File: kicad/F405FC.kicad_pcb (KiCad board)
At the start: 4 copper layers, 36 x 36 mm, 161 parts, among them J1 USB4105-GF-A, J2 ESC, J3 HD VTX, J4 GPS, J5 ELRS, P1 VBAT, P10 LED_DIN, P11 5V, P12 GND, P13 5V, P14 BUZ_N, P15 UART5_TX, P16 UART5_RX, P17 UART6_TX, P18 UART6_RX, P19 MOTOR5, P2 GND, P20 MOTOR6, P21 MOTOR7, P22 MOTOR8, P23 RSSI_IN, P24 GND, P25 5V, P3 10V, P4 GND, P5 CAM1_VID, P6 CAM2_VID, P7 VTX_VID, P8 5V, P9 GND, Q1 PMV40UN2, Q2 NX7002AK, SW1 BOOT, U1 LMR38020FSDDAR, U10 W25N01GV, U11 TS5A3159A, U12 SN74LV1T125, U13 USBLC6-2SC6, U2 LMR38020FSDDAR, U3 STM32F405RGT6, U4 LP38692MP-3.3, U5 LP5907MFX-3.3, U6 ICM-42688-P, U7 BMI270, U8 BMP390, U9 IIS2MDC, Y1 8MHz

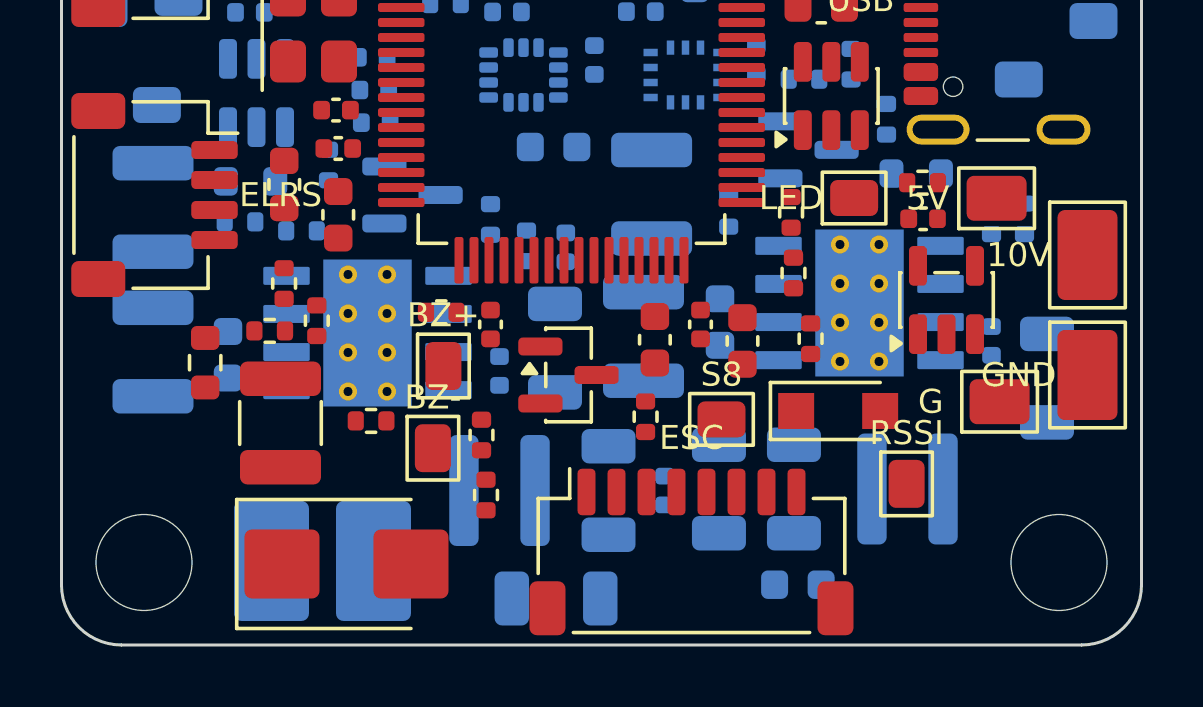
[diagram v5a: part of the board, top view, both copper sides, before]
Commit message: Routing prep: scripted critical buck/VBAT routes (gen/critical.py), BST caps rotated, DRC position helper
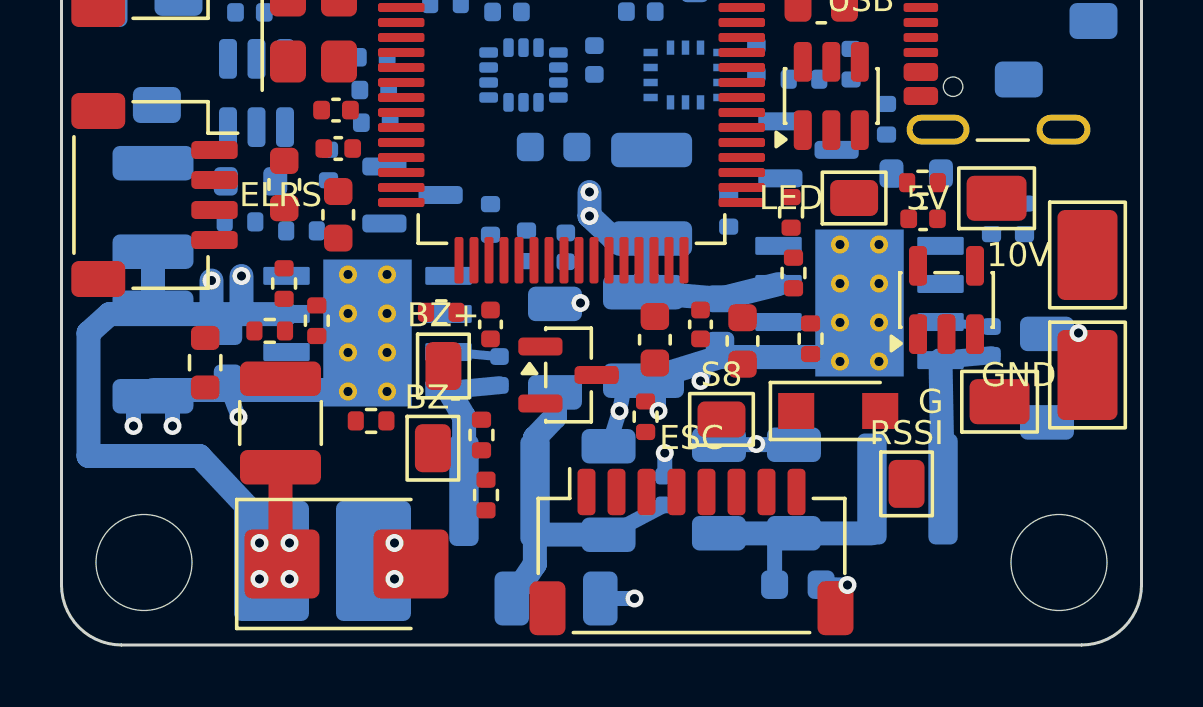
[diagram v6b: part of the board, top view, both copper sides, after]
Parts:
- turned C13 to -90 degrees
- turned C5 to -90 degrees
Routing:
- net VBAT: track 0.00 -> 48.1 mm, vias 0 -> 8
- net GND: track 0.00 -> 26.6 mm, vias 0 -> 14
- net 5V: track 0.00 -> 10.5 mm
- net 10V: track 0.00 -> 6.81 mm
- net SW_10V: track 0.00 -> 6.01 mm
- net SW_5V: track 0.00 -> 5.20 mm
- net BST_5V: track 0.00 -> 1.71 mm
- net BST_10V: track 0.00 -> 1.71 mm
- added copper zone on In1.Cu, net GND

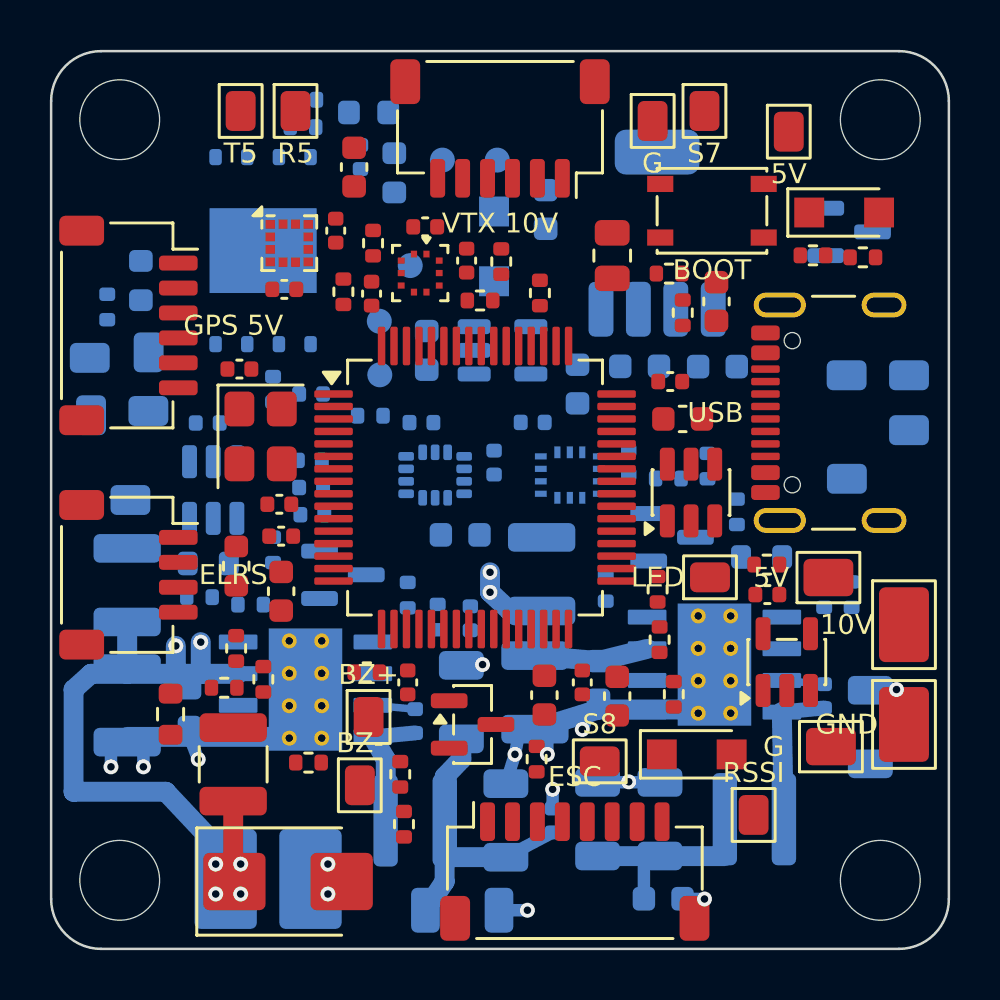
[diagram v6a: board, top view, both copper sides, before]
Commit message: Routing infrastructure: DRC rules persisted to .kicad_pro, GND fanout (gen/gndfan.py), In1 kept signal-free in DSN, output script, assembly/bring-up guide draft
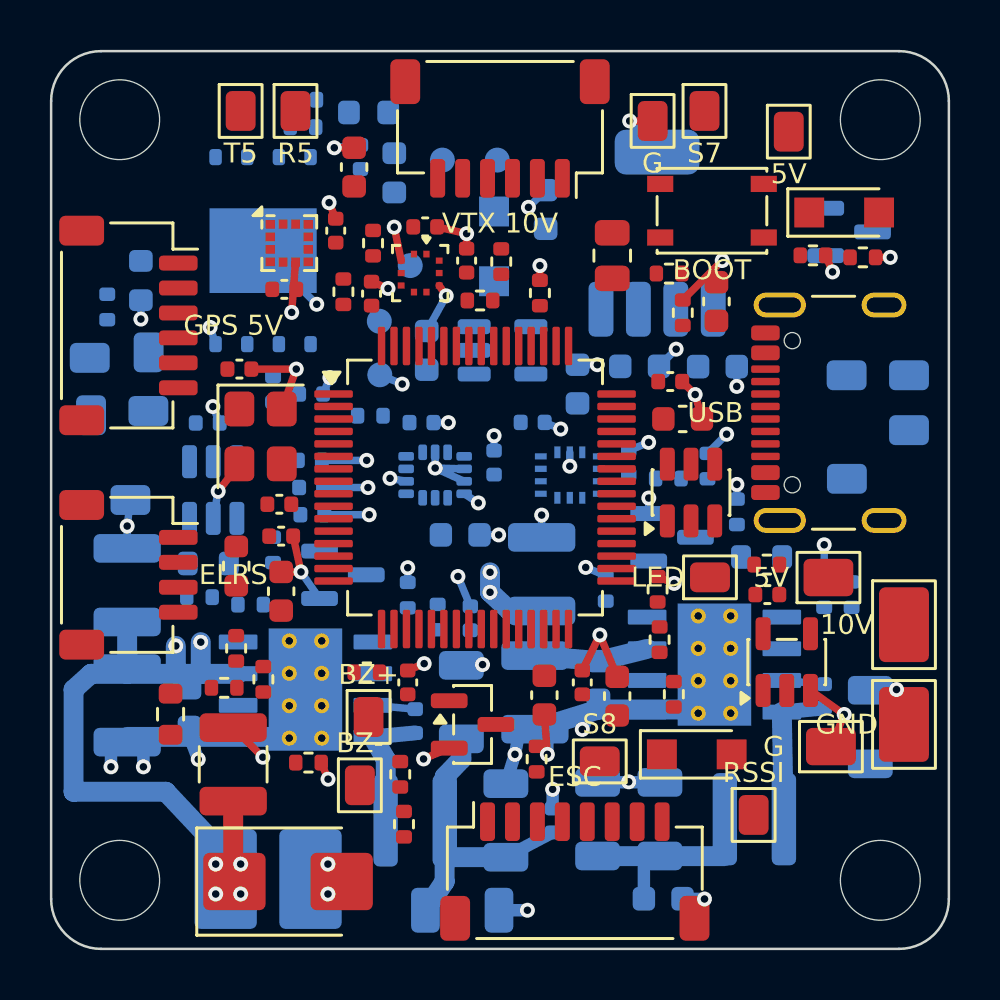
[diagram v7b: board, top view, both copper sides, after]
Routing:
- net GND: track 26.6 -> 108.1 mm, vias 14 -> 68
- removed copper zone on In1.Cu, net GND

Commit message: Routing: MCU inward fanout, rip-up-and-reroute finisher (gen/ripup.py), maze router, geometry export/apply, provisional IMU alignment + FRONT silk
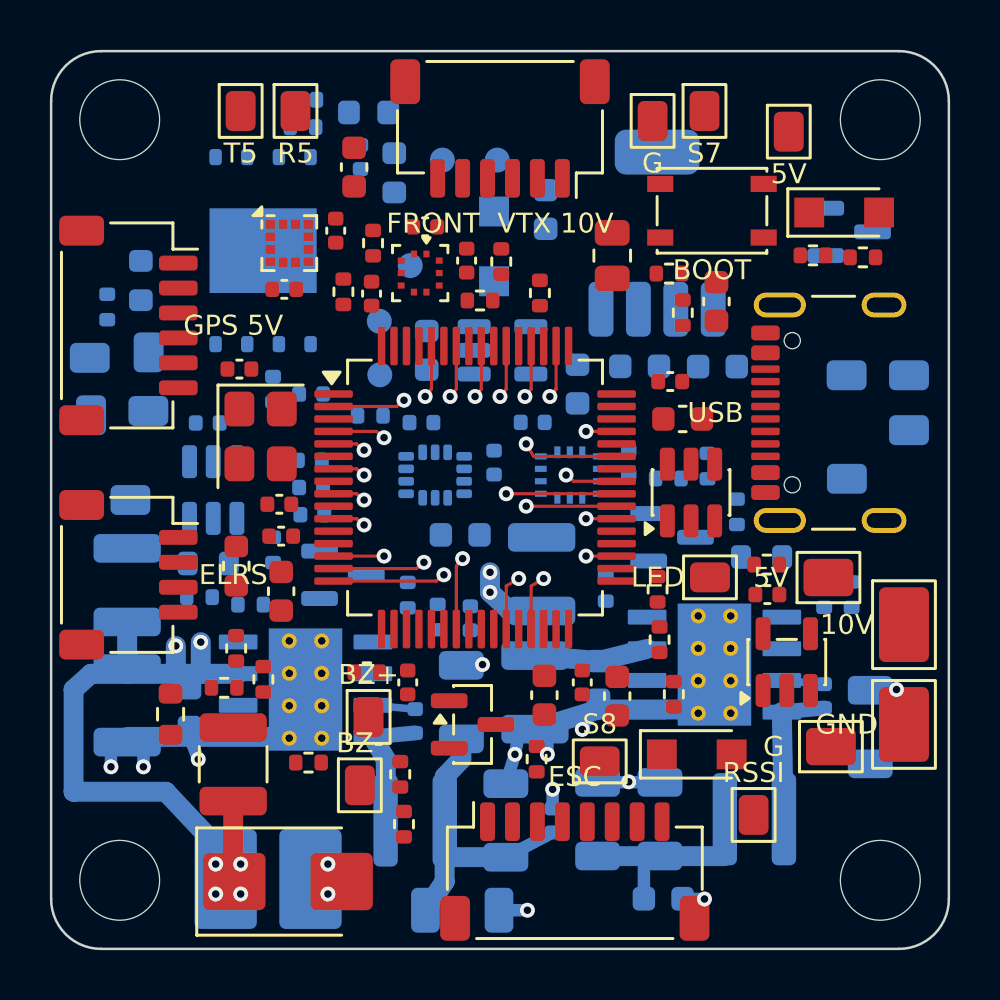
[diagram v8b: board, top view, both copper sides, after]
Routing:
- net GND: track 108.1 -> 26.6 mm, vias 68 -> 14
- net UART2_TX: track 0.00 -> 4.52 mm, vias 0 -> 1
- net MOTOR6: track 0.00 -> 4.42 mm, vias 0 -> 1
- net UART1_RX: track 0.00 -> 3.91 mm, vias 0 -> 1
- net ESC_TLM: track 0.00 -> 3.72 mm, vias 0 -> 1
- net MOTOR5: track 0.00 -> 3.62 mm, vias 0 -> 1
- net CAM_SEL: track 0.00 -> 2.92 mm, vias 0 -> 1
- net SPI1_MOSI: track 0.00 -> 2.92 mm, vias 0 -> 1
- net MOTOR3: track 0.00 -> 2.31 mm, vias 0 -> 1
- net MOTOR2: track 0.00 -> 2.31 mm, vias 0 -> 1
- net VTX_PWR_EN: track 0.00 -> 2.12 mm, vias 0 -> 1
- net UART5_RX: track 0.00 -> 2.12 mm, vias 0 -> 1
- net UART3_RX: track 0.00 -> 2.12 mm, vias 0 -> 1
- net SPI3_MISO: track 0.00 -> 2.12 mm, vias 0 -> 1
- net GYRO2_CS: track 0.00 -> 2.12 mm, vias 0 -> 1
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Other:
- board text added: "FRONT VTX 10V"
- board text removed: "VTX 10V"
